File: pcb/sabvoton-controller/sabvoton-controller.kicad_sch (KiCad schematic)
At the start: 29 parts, among them J1 Conn_02x03_Counter_Clockwise, J2 Conn_01x30, U1 ESP32-WROOM-32, U2 XL7015E1, U3 XL7015E1, U4 NCP1117-3.3_SOT223, U5 LM1117-1.8

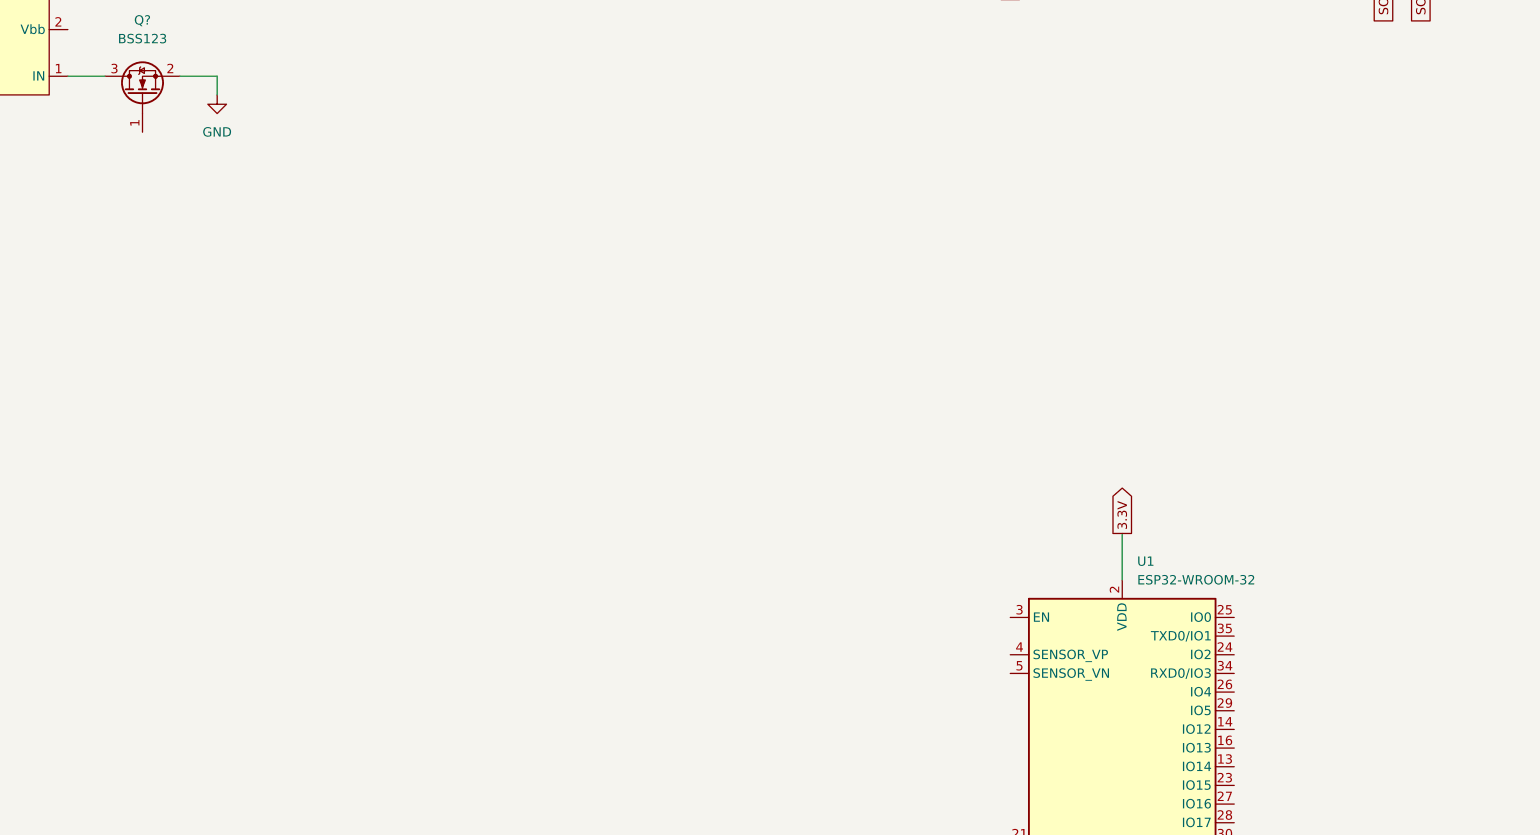
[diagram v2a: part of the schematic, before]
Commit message: Connect power switch to the esp
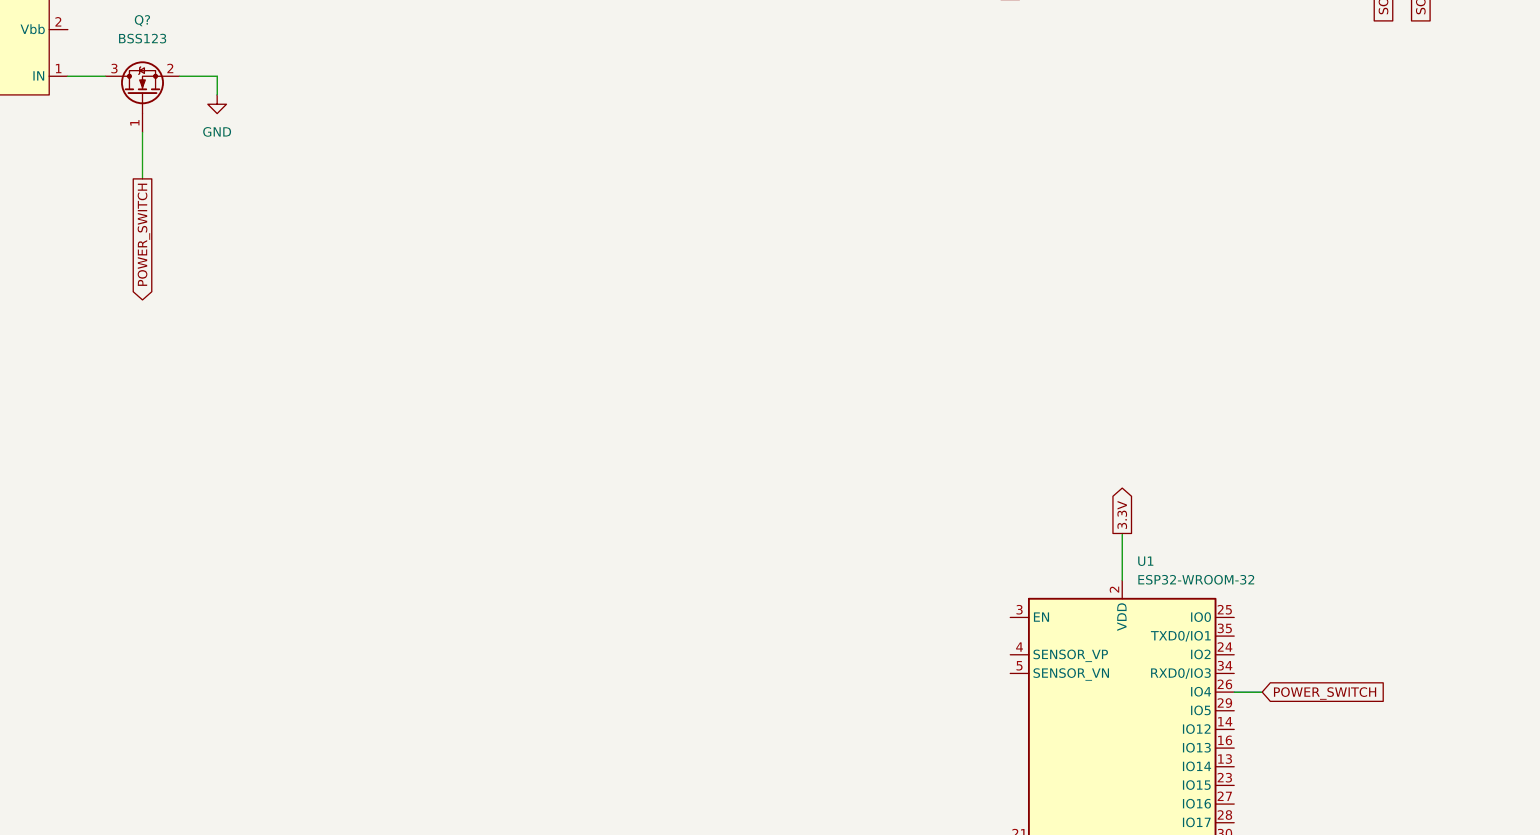
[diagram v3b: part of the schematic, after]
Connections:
- net POWER_SWITCH: now reaches Q?.1 (G)
- net POWER_SWITCH: now also U1.26 (IO4)
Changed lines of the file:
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@@
+    (stroke (width 0) (type default) (color 0 0 0 0))
+  )
+  (wire (pts (xy 259.08 96.52) (xy 259.08 102.87))
     (stroke (width 0) (type default) (color 0 0 0 0))
   )
@@
     (stroke (width 0) (type default) (color 0 0 0 0))
   )
+  (wire (pts (xy 407.67 172.72) (xy 411.48 172.72))
+    (stroke (width 0) (type default) (color 0 0 0 0))
+  )
   (wire (pts (xy 496.57 74.93) (xy 501.65 74.93))
     (stroke (width 0) (type default) (color 0 0 0 0))
@@
     )
   )
+  (global_label "POWER_SWITCH" (shape input) (at 411.48 172.72 0) (fields_autoplaced)
+    (effects (font (size 1.27 1.27)) (justify left))
+    (property "Intersheet References" "${INTERSHEET_REFS}" (id 0) (at 428.1655 172.6406 0)
+      (effects (font (size 1.27 1.27)) (justify left) hide)
+    )
+  )
   (global_label "3.3V" (shape input) (at 598.17 55.88 0) (fields_autoplaced)
     (effects (font (size 1.27 1.27)) (justify left))
@@
     )
   )
+  (global_label "POWER_SWITCH" (shape output) (at 259.08 102.87 270) (fields_autoplaced)
+    (effects (font (size 1.27 1.27)) (justify right))
+    (property "Intersheet References" "${INTERSHEET_REFS}" (id 0) (at 259.0006 119.5555 90)
+      (effects (font (size 1.27 1.27)) (justify right) hide)
+    )
+  )

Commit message: Added battery voltage input
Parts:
- added J?: ENGINE_HALL, symbol Connector_Generic:Conn_01x06
- added RB1: 56k, Resistor_SMD:R_1206_3216Metric_Pad1.30x1.75mm_HandSolder, symbol Device:R
- added RB2: 1M, Resistor_SMD:R_1206_3216Metric_Pad1.30x1.75mm_HandSolder, symbol Device:R
- J1: value Conn_02x03_Counter_Clockwise -> CONTROLLER_HALL
- J2: value Conn_01x30 -> CONN_MAIN
- gave numbers to parts that had none: 2
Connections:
- net B+: now also RB2.2
- net GND: now also RB1.2
- net BATTERY_VOLTAGE: now reaches U1.7 (IO35)
- net BATTERY_VOLTAGE: now also RB1.1, RB2.1
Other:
- moved on the sheet: J1, U1

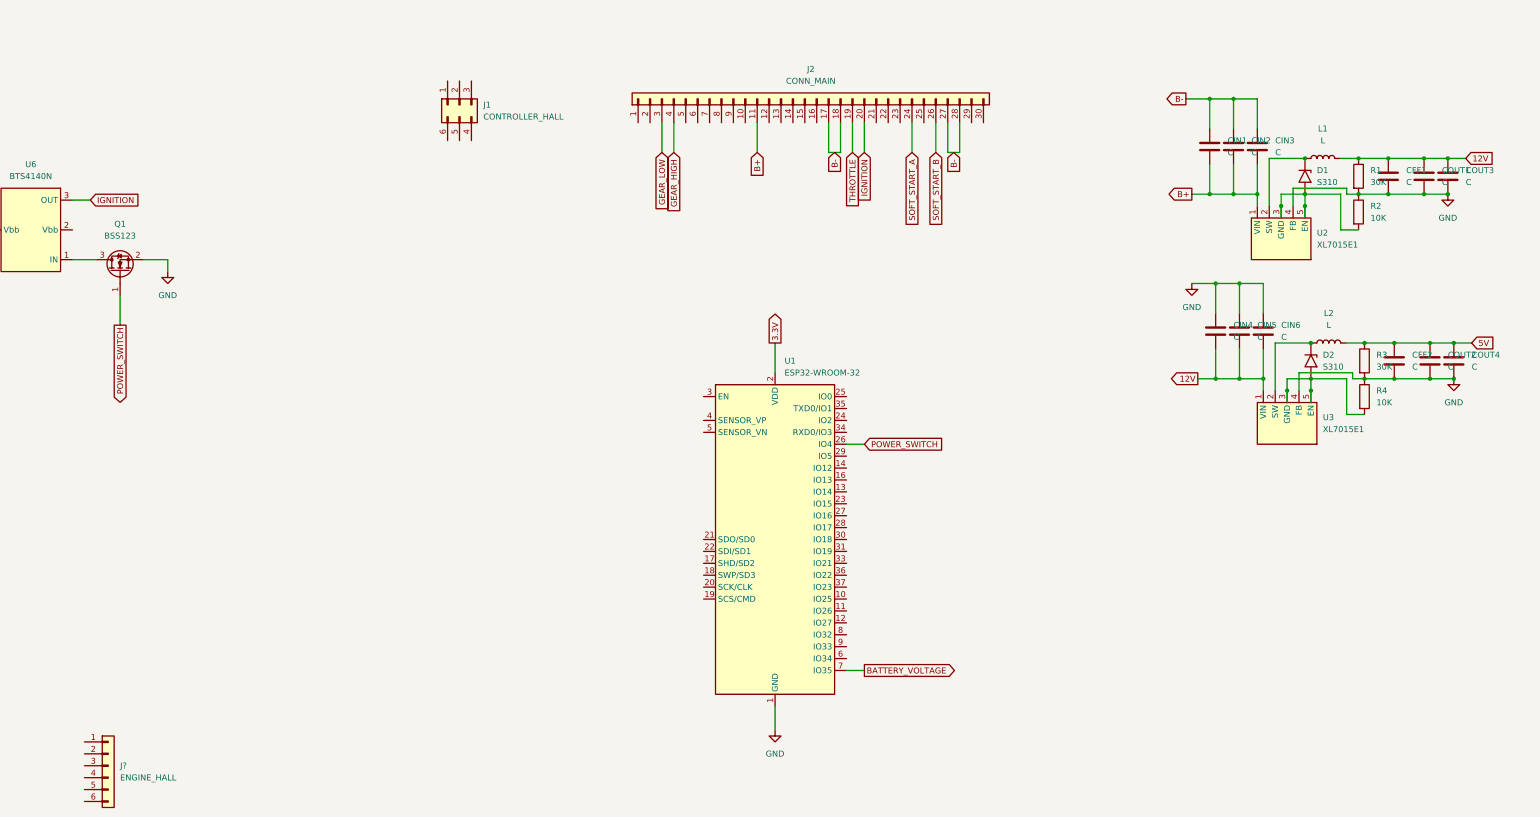
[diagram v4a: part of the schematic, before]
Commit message: Added engine temperature & speed sensor
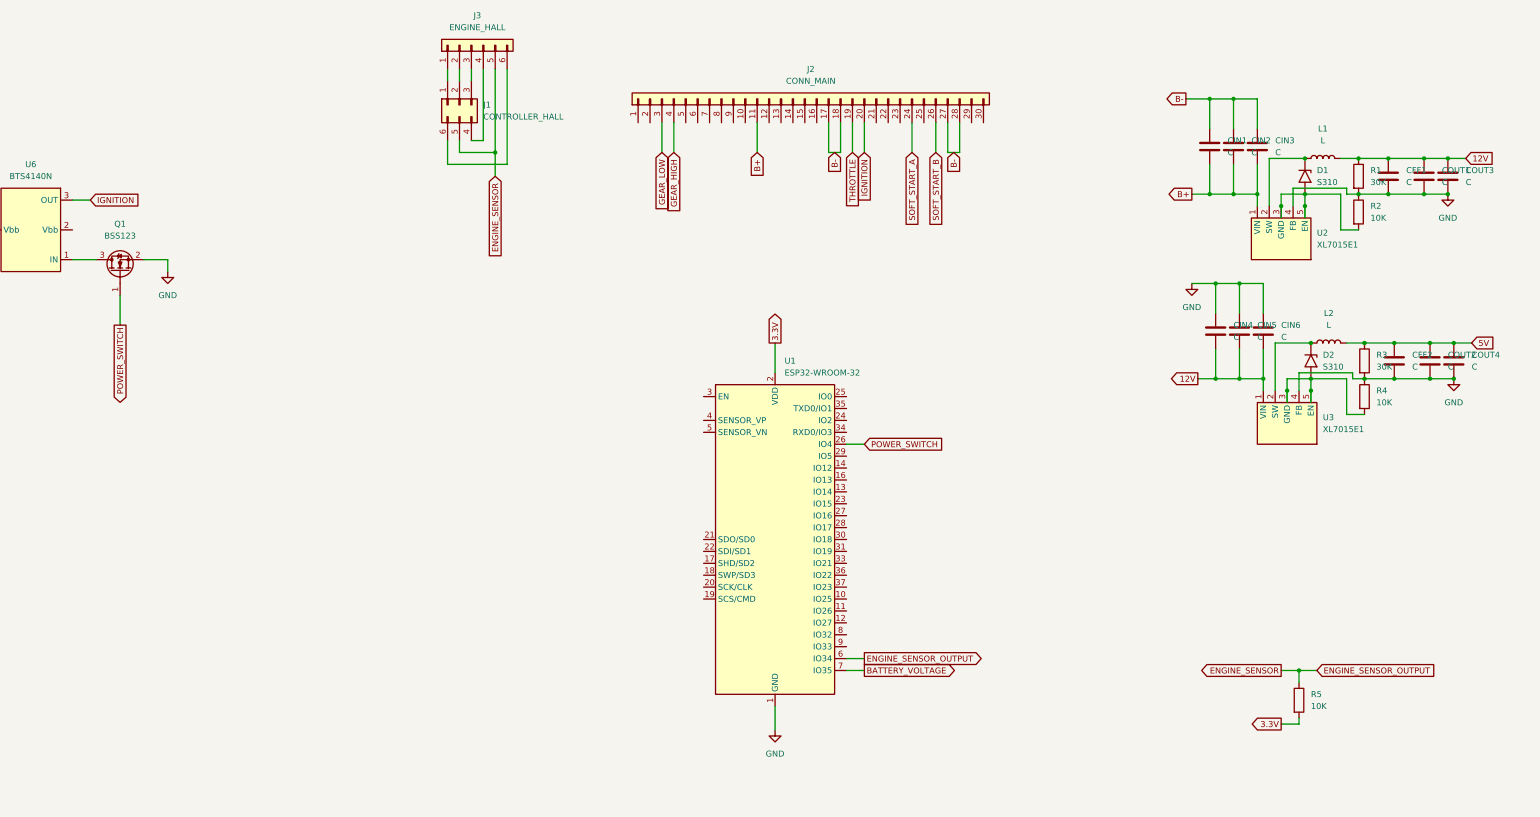
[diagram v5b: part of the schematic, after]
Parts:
- added R5: 10K, symbol Device:R
- gave numbers to parts that had none: 1
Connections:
- net 3.3V: now also R5.2
- net at J3.1 (Pin_1): now also J1.1 (Pin_1)
- net at J3.2 (Pin_2): now also J1.2 (Pin_2)
- net at J3.3 (Pin_3): now also J1.3 (Pin_3)
- net at J3.4 (Pin_4): now also J1.4 (Pin_4)
- net ENGINE_SENSOR: now reaches J3.5 (Pin_5)
- net ENGINE_SENSOR: now also J1.5 (Pin_5), U1.6 (IO34), R5.1
- net at J3.6 (Pin_6): now also J1.6 (Pin_6)
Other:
- moved on the sheet: J3
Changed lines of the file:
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@@
   (junction (at 511.81 74.93) (diameter 0) (color 0 0 0 0)
   )
+  (junction (at 510.54 176.53) (diameter 0) (color 0 0 0 0)
+  )
   (junction (at 537.21 74.93) (diameter 0) (color 0 0 0 0)
   )
@@
   (junction (at 491.49 74.93) (diameter 0) (color 0 0 0 0)
   )
+  (junction (at 339.09 66.04) (diameter 0) (color 0 0 0 0)
+  )
   (junction (at 508 116.84) (diameter 0) (color 0 0 0 0)
   )
@@
     (stroke (width 0) (type default) (color 0 0 0 0))
   )
+  (wire (pts (xy 341.63 68.58) (xy 341.63 48.26))
+    (stroke (width 0) (type default) (color 0 0 0 0))
+  )
+  (wire (pts (xy 334.01 63.5) (xy 336.55 63.5))
+    (stroke (width 0) (type default) (color 0 0 0 0))
+  )
   (wire (pts (xy 524.51 114.3) (xy 530.86 114.3))
     (stroke (width 0) (type default) (color 0 0 0 0))
@@
     (stroke (width 0) (type default) (color 0 0 0 0))
   )
+  (wire (pts (xy 506.73 187.96) (xy 510.54 187.96))
+    (stroke (width 0) (type default) (color 0 0 0 0))
+  )
+  (wire (pts (xy 510.54 176.53) (xy 514.35 176.53))
+    (stroke (width 0) (type default) (color 0 0 0 0))
+  )
   (wire (pts (xy 510.54 113.03) (xy 521.97 113.03))
     (stroke (width 0) (type default) (color 0 0 0 0))
@@
     (stroke (width 0) (type default) (color 0 0 0 0))
   )
+  (wire (pts (xy 331.47 63.5) (xy 331.47 66.04))
+    (stroke (width 0) (type default) (color 0 0 0 0))
+  )
   (wire (pts (xy 624.84 50.8) (xy 629.92 50.8))
     (stroke (width 0) (type default) (color 0 0 0 0))
@@
     (stroke (width 0) (type default) (color 0 0 0 0))
   )
+  (wire (pts (xy 328.93 48.26) (xy 328.93 50.8))
+    (stroke (width 0) (type default) (color 0 0 0 0))
+  )
   (wire (pts (xy 497.84 93.98) (xy 497.84 100.33))
     (stroke (width 0) (type default) (color 0 0 0 0))
@@
     (stroke (width 0) (type default) (color 0 0 0 0))
   )
+  (wire (pts (xy 334.01 48.26) (xy 334.01 50.8))
+    (stroke (width 0) (type default) (color 0 0 0 0))
+  )
   (wire (pts (xy 491.49 68.58) (xy 491.49 74.93))
     (stroke (width 0) (type default) (color 0 0 0 0))
   )
+  (wire (pts (xy 510.54 176.53) (xy 510.54 179.07))
+    (stroke (width 0) (type default) (color 0 0 0 0))
+  )
+  (wire (pts (xy 339.09 66.04) (xy 339.09 71.12))
+    (stroke (width 0) (type default) (color 0 0 0 0))
+  )
   (wire (pts (xy 530.86 106.68) (xy 538.48 106.68))
     (stroke (width 0) (type default) (color 0 0 0 0))
@@
     (stroke (width 0) (type default) (color 0 0 0 0))
   )
+  (wire (pts (xy 328.93 63.5) (xy 328.93 68.58))
+    (stroke (width 0) (type default) (color 0 0 0 0))
+  )
   (wire (pts (xy 519.43 67.31) (xy 523.24 67.31))
     (stroke (width 0) (type default) (color 0 0 0 0))
@@
     (stroke (width 0) (type default) (color 0 0 0 0))
   )
+  (wire (pts (xy 336.55 63.5) (xy 336.55 48.26))
+    (stroke (width 0) (type default) (color 0 0 0 0))
+  )
   (wire (pts (xy 417.83 59.69) (xy 417.83 66.04))
     (stroke (width 0) (type default) (color 0 0 0 0))
@@
     (stroke (width 0) (type default) (color 0 0 0 0))
   )
+  (wire (pts (xy 328.93 68.58) (xy 341.63 68.58))
+    (stroke (width 0) (type default) (color 0 0 0 0))
+  )
+  (wire (pts (xy 331.47 48.26) (xy 331.47 50.8))
+    (stroke (width 0) (type default) (color 0 0 0 0))
+  )
   (wire (pts (xy 497.84 107.95) (xy 497.84 114.3))
     (stroke (width 0) (type default) (color 0 0 0 0))
@@
     (stroke (width 0) (type default) (color 0 0 0 0))
   )
+  (wire (pts (xy 510.54 187.96) (xy 510.54 186.69))
+    (stroke (width 0) (type default) (color 0 0 0 0))
+  )
   (wire (pts (xy 519.43 82.55) (xy 519.43 74.93))
     (stroke (width 0) (type default) (color 0 0 0 0))
   )
+  (wire (pts (xy 506.73 176.53) (xy 510.54 176.53))
+    (stroke (width 0) (type default) (color 0 0 0 0))
+  )
   (wire (pts (xy 523.24 74.93) (xy 529.59 74.93))
     (stroke (width 0) (type default) (color 0 0 0 0))
@@
     (stroke (width 0) (type default) (color 0 0 0 0))
   )
+  (wire (pts (xy 339.09 66.04) (xy 339.09 48.26))
+    (stroke (width 0) (type default) (color 0 0 0 0))
+  )
   (wire (pts (xy 398.78 106.68) (xy 398.78 113.03))
     (stroke (width 0) (type default) (color 0 0 0 0))
@@
     (stroke (width 0) (type default) (color 0 0 0 0))
   )
+  (wire (pts (xy 331.47 66.04) (xy 339.09 66.04))
+    (stroke (width 0) (type default) (color 0 0 0 0))
+  )
+  (wire (pts (xy 414.02 173.99) (xy 417.83 173.99))
+    (stroke (width 0) (type default) (color 0 0 0 0))
+  )
   (wire (pts (xy 435.61 59.69) (xy 435.61 66.04))
     (stroke (width 0) (type default) (color 0 0 0 0))
+  )
+  (global_label "ENGINE_SENSOR" (shape input) (at 339.09 71.12 270) (fields_autoplaced)
+    (effects (font (size 1.27 1.27)) (justify right))
+    (property "Intersheet References" "${INTERSHEET_REFS}" (id 0) (at 339.0106 88.8336 90)
+      (effects (font (size 1.27 1.27)) (justify right) hide)
+    )
   )
   (global_label "3.3V" (shape output) (at 398.78 106.68 90) (fields_autoplaced)
@@
     )
   )
+  (global_label "3.3V" (shape output) (at 506.73 187.96 180) (fields_autoplaced)
+    (effects (font (size 1.27 1.27)) (justify right))
+    (property "Intersheet References" "${INTERSHEET_REFS}" (id 0) (at 500.2045 187.8806 0)
+      (effects (font (size 1.27 1.27)) (justify right) hide)
+    )
+  )
   (global_label "12V" (shape output) (at 488.95 114.3 180) (fields_autoplaced)
     (effects (font (size 1.27 1.27)) (justify right))
@@
     )
   )
+  (global_label "ENGINE_SENSOR_OUTPUT" (shape input) (at 514.35 176.53 0) (fields_autoplaced)
+    (effects (font (size 1.27 1.27)) (justify left))
+    (property "Intersheet References" "${INTERSHEET_REFS}" (id 0) (at 540.2279 176.4506 0)
+      (effects (font (size 1.27 1.27)) (justify left) hide)
+    )
+  )
   (global_label "B+" (shape input) (at 394.97 66.04 270) (fields_autoplaced)
     (effects (font (size 1.27 1.27)) (justify right))
@@
     )
   )
+  (global_label "ENGINE_SENSOR_OUTPUT" (shape output) (at 417.83 173.99 0) (fields_autoplaced)
+    (effects (font (size 1.27 1.27)) (justify left))
+    (property "Intersheet References" "${INTERSHEET_REFS}" (id 0) (at 443.7079 173.9106 0)
+      (effects (font (size 1.27 1.27)) (justify left) hide)
+    )
+  )
   (global_label "SOFT_START_B" (shape input) (at 433.07 66.04 270) (fields_autoplaced)
     (effects (font (size 1.27 1.27)) (justify right))
@@
     )
   )
+  (global_label "ENGINE_SENSOR" (shape output) (at 506.73 176.53 180) (fields_autoplaced)
+    (effects (font (size 1.27 1.27)) (justify right))
+    (property "Intersheet References" "${INTERSHEET_REFS}" (id 0) (at 489.0164 176.4506 0)
+      (effects (font (size 1.27 1.27)) (justify right) hide)
+    )
+  )
   (global_label "BATTERY_VOLTAGE" (shape output) (at 417.83 176.53 0) (fields_autoplaced)
     (effects (font (size 1.27 1.27)) (justify left))
@@
     (pin "2")
   )
-  (symbol (lib_id "Connector_Generic:Conn_01x06") (at 256.54 196.85 0) (unit 1)
-    (in_bom yes) (on_board yes) (fields_autoplaced)
-    (property "Reference" "J?" (id 0) (at 259.08 196.8499 0)
-      (effects (font (size 1.27 1.27)) (justify left))
-    )
-    (property "Value" "ENGINE_HALL" (id 1) (at 259.08 199.3899 0)
-      (effects (font (size 1.27 1.27)) (justify left))
-    )
-    (property "Footprint" "" (id 2) (at 256.54 196.85 0)
-      (effects (font (size 1.27 1.27)) hide)
-    )
-    (property "Datasheet" "~" (id 3) (at 256.54 196.85 0)
+  (symbol (lib_id "Connector_Generic:Conn_01x06") (at 334.01 43.18 90) (unit 1)
+    (in_bom yes) (on_board yes) (fields_autoplaced)
+    (property "Reference" "J3" (id 0) (at 335.28 36.83 90))
+    (property "Value" "ENGINE_HALL" (id 1) (at 335.28 39.37 90))
+    (property "Footprint" "" (id 2) (at 334.01 43.18 0)
+      (effects (font (size 1.27 1.27)) hide)
+    )
+    (property "Datasheet" "~" (id 3) (at 334.01 43.18 0)
       (effects (font (size 1.27 1.27)) hide)
     )
@@
     )
     (property "Datasheet" "~" (id 3) (at 538.48 110.49 0)
+      (effects (font (size 1.27 1.27)) hide)
+    )
+    (pin "1")
+    (pin "2")
+  )
+  (symbol (lib_id "Device:R") (at 510.54 182.88 0) (unit 1)
+    (in_bom yes) (on_board yes) (fields_autoplaced)
+    (property "Reference" "R5" (id 0) (at 513.08 181.6099 0)
+      (effects (font (size 1.27 1.27)) (justify left))
+    )
+    (property "Value" "10K" (id 1) (at 513.08 184.1499 0)
+      (effects (font (size 1.27 1.27)) (justify left))
+    )
+    (property "Footprint" "" (id 2) (at 508.762 182.88 90)
+      (effects (font (size 1.27 1.27)) hide)
+    )
+    (property "Datasheet" "~" (id 3) (at 510.54 182.88 0)
       (effects (font (size 1.27 1.27)) hide)
     )
@@
     )
     (path "/447c4405-a559-489c-a0e1-220611203f13"
-      (reference "J?") (unit 1) (value "ENGINE_HALL") (footprint "")
+      (reference "J3") (unit 1) (value "ENGINE_HALL") (footprint "")
     )
     (path "/b150b223-b6c5-46e4-b2eb-a749cfde889d"
@@
       (reference "R4") (unit 1) (value "10K") (footprint "Resistor_SMD:R_1206_3216Metric_Pad1.30x1.75mm_HandSolder")
     )
+    (path "/8019f8b8-7278-4d90-a244-edd6b916cf16"
+      (reference "R5") (unit 1) (value "10K") (footprint "")
+    )
     (path "/d6f841e6-b958-49b1-a72e-7ccce9ff65ec"
